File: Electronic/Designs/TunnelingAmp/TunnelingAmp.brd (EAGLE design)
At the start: 35 x 25 mm, 8 parts, among them U1 OPA627AUE4

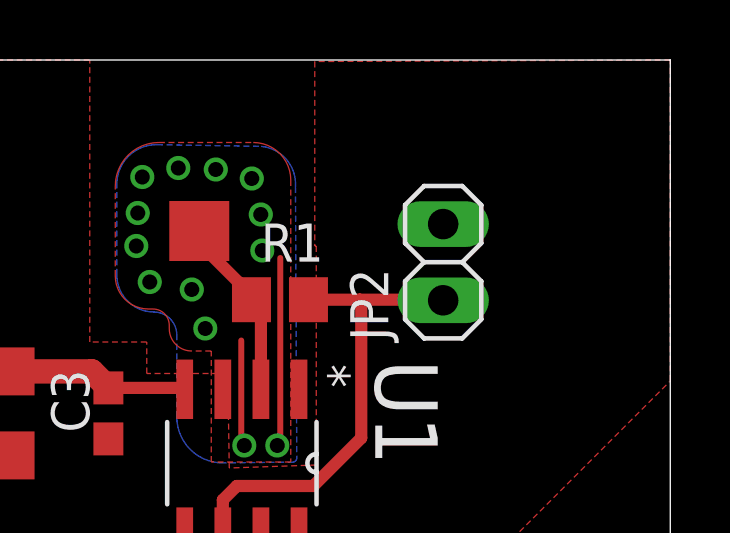
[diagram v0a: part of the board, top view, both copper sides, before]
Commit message: moved silkscreen text in ADC
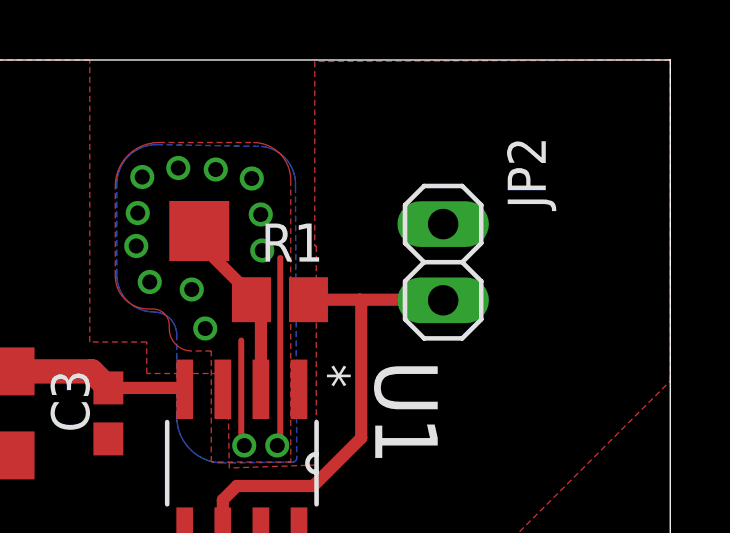
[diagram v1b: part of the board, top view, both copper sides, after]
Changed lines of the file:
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@@
 <element name="C4" library="resistor" package="C0603" value="100nf" x="20.5" y="6.17" rot="R180"/>
 <element name="JP1" library="pinhead" package="1X04" value="pwr" x="7.38" y="9.41" rot="R90"/>
-<element name="JP2" library="pinhead" package="1X02" value="out" x="27.43" y="18.26" rot="R90"/>
+<element name="JP2" library="pinhead" package="1X02" value="out" x="27.43" y="18.26" smashed="yes" rot="R90">
+<attribute name="NAME" x="30.8512" y="20.0438" size="1.27" layer="25" ratio="10" rot="R90"/>
+<attribute name="VALUE" x="30.605" y="15.72" size="1.27" layer="27" rot="R90"/>
+</element>
 <element name="R1" library="resistor" package="R0805" value="100M" x="21.99" y="17.01"/>
 <element name="U1" library="OPA627_FromFarnell" package="SOIC127P600X175-8N" value="OPA627AUE4" x="20.72" y="11.56" rot="R270">
